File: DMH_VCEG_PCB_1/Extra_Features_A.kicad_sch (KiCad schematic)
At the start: 13 parts, among them U4 CD4066BE, U8 TL074

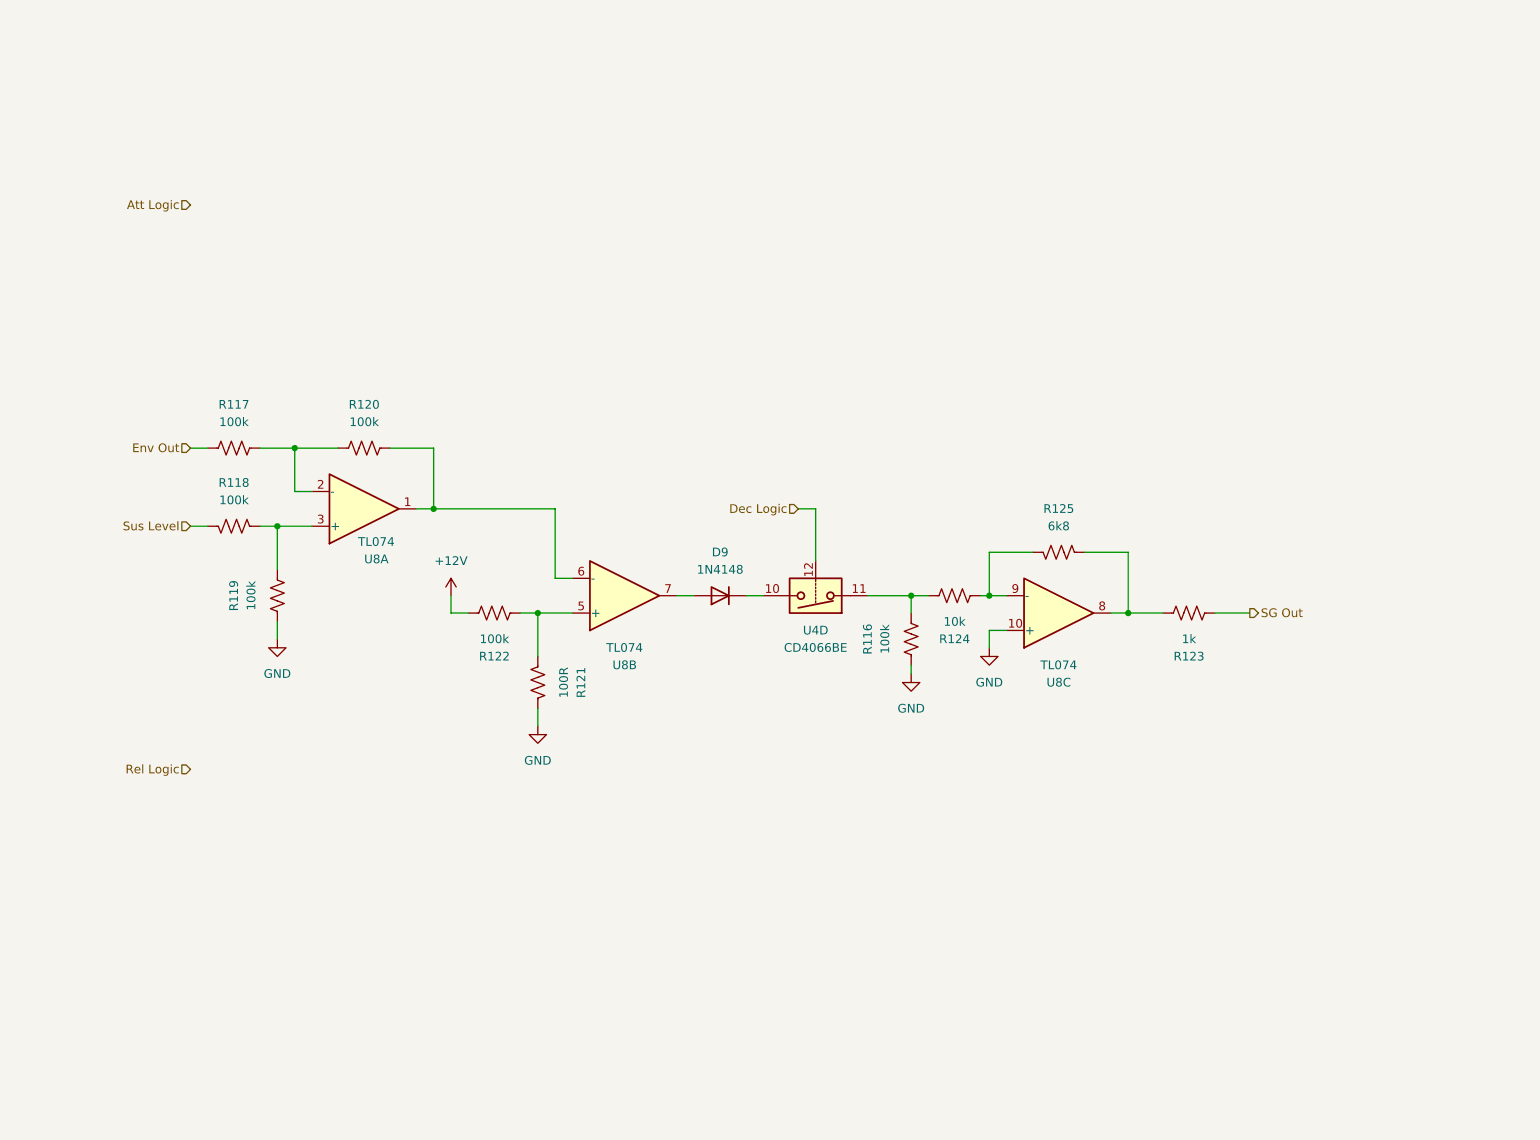
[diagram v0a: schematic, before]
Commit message: Implemented LEDs
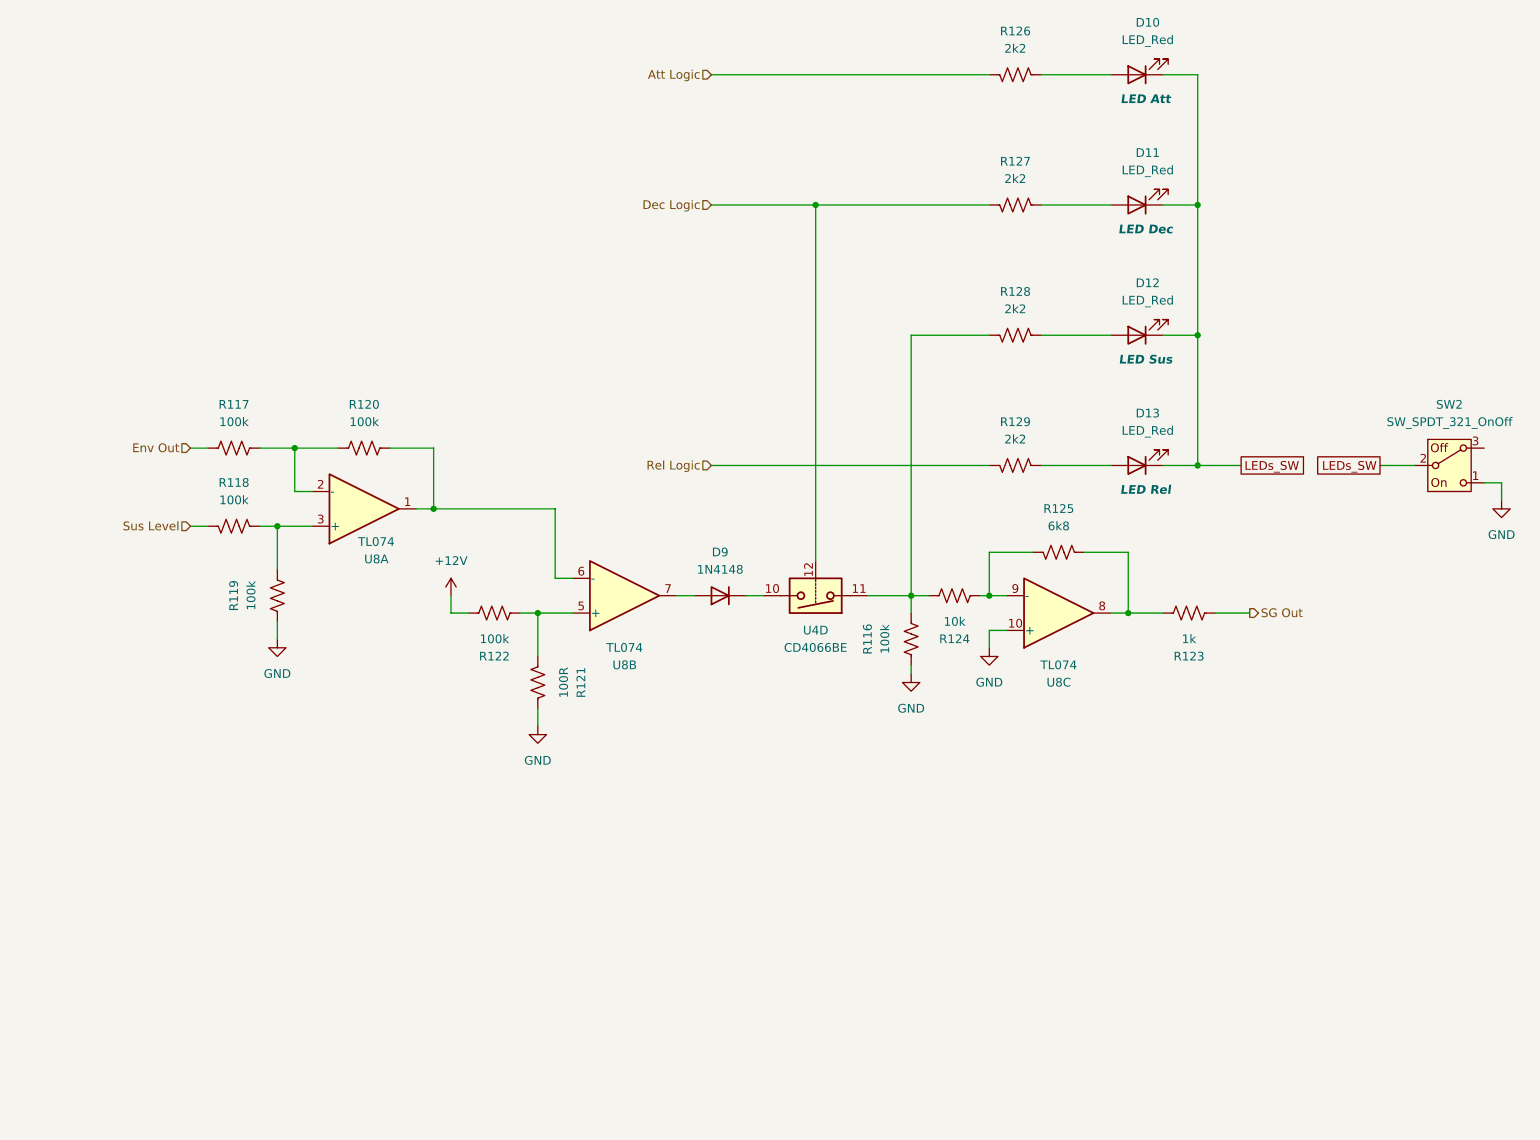
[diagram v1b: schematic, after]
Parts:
- added D10, D11, D12, D13: LED_Red, LED_THT:LED_D3.0mm, symbol Device:LED
- added R126, R127, R128, R129: 2k2, Resistor_THT:R_Axial_DIN0207_L6.3mm_D2.5mm_P7.62mm_Horizontal, symbol Device:R_US
- added SW2: SW_SPDT_321_OnOff, SynthStuff:Toggle_Switch_THT, symbol SynthStuff:SW_SPDT_321_OnOff
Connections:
- net Att Logic: now also R126.1
- net Dec Logic: now also R127.1
- net GND: now also SW2.1 (C)
- net Rel Logic: now also R129.1
- net at R116.1, R124.1, U4.11: now also R128.1
- new net: D10.2 (A), R126.2
- new net: D11.2 (A), R127.2
- new net: D13.2 (A), R129.2
- new net: D12.2 (A), R128.2
- new net LEDs_SW: D10.1 (K), D11.1 (K), D12.1 (K), D13.1 (K), SW2.2 (B)

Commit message: Added Out R
Ready for breadboarding
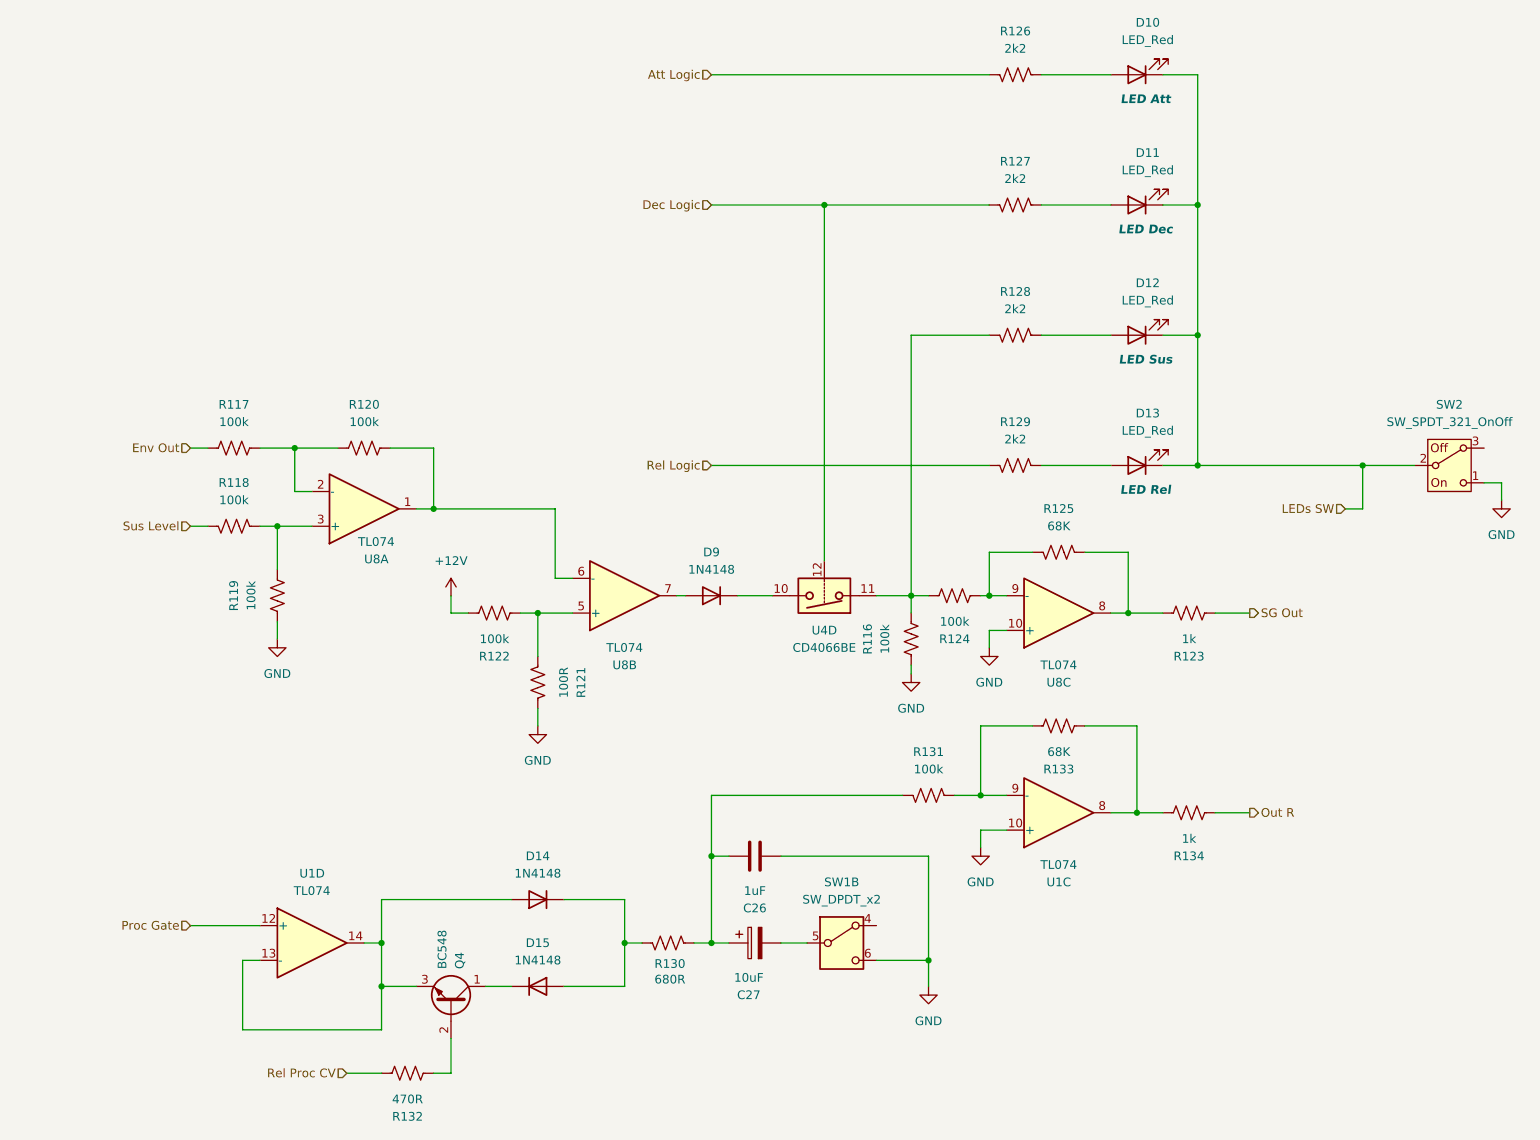
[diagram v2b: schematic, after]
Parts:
- added C26: 1uF, Capacitor_THT:C_Disc_D4.3mm_W1.9mm_P5.00mm, symbol Device:C
- added C27: 10uF, Capacitor_THT:CP_Radial_D5.0mm_P2.00mm, symbol Device:C_Polarized
- added D14, D15: 1N4148, Diode_THT:D_DO-35_SOD27_P7.62mm_Horizontal, symbol Diode:1N4148
- added Q4: BC548, Package_TO_SOT_THT:TO-92L_Inline_Wide, symbol Transistor_BJT:BC548
- added R130: 680R, Resistor_THT:R_Axial_DIN0207_L6.3mm_D2.5mm_P7.62mm_Horizontal, symbol Device:R_US
- added R131: 100k, Resistor_THT:R_Axial_DIN0207_L6.3mm_D2.5mm_P7.62mm_Horizontal, symbol Device:R_US
- added R132: 470R, Resistor_THT:R_Axial_DIN0207_L6.3mm_D2.5mm_P7.62mm_Horizontal, symbol Device:R_US
- added R133: 68K, Resistor_THT:R_Axial_DIN0207_L6.3mm_D2.5mm_P7.62mm_Horizontal, symbol Device:R_US
- added R134: 1k, Resistor_THT:R_Axial_DIN0207_L6.3mm_D2.5mm_P7.62mm_Horizontal, symbol Device:R_US
- added SW1: SW_DPDT_x2, symbol Switch:SW_DPDT_x2
- added U1: TL074, symbol Amplifier_Operational:TL074
- R124: value 10k -> 100k
- R125: value 6k8 -> 68K
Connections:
- net GND: now also C26.2, SW1.6 (C), U1.10 (+)
- net LEDs_SW renamed LEDs SW
- new net: D15.1 (K), Q4.1 (C)
- new net: D14.1 (K), D15.2 (A), R130.2
- new net: C26.1, C27.1, R130.1, R131.1
- new net: C27.2, SW1.5 (B)
- new net: Q4.2 (B), R132.2
- new net: R131.2, R133.1, U1.9 (-)
- new net: D14.2 (A), Q4.3 (E), U1.13 (-), U1.14
- new net: R133.2, R134.1, U1.8
- new net Out R: R134.2
- new net Proc Gate: U1.12 (+)
- new net Rel Proc CV: R132.1
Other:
- moved on the sheet: D9, U4D

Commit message: Corrected Out R design
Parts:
- removed D15: 1N4148, Diode_THT:D_DO-35_SOD27_P7.62mm_Horizontal, symbol Diode:1N4148
- added R2, R4: 100k, Resistor_THT:R_Axial_DIN0207_L6.3mm_D2.5mm_P7.62mm_Horizontal, symbol Device:R_US
- added U3: 40106, symbol 4xxx:40106
- SW2: footprint SynthStuff:Toggle_Switch_THT -> SynthStuff:Toggle_Switch_TE
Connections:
- net GND: now also U1.10 (+), U1.12 (+); no longer U1.10 (+)
- net Proc Gate: now also U3.3; no longer U1.12 (+)
- net at Q4.1 (C): now also D14.1 (K), R130.2
- net at R131.2, R133.1: now also U1.13 (-); no longer U1.9 (-)
- net at D14.2 (A), Q4.3 (E): now also U3.6; no longer U1.13 (-), U1.14
- new net: R134.1, R4.2, U1.8
- new net: R2.2, R4.1, U1.9 (-)
- new net: R133.2, R2.1, U1.14
- new net: U3.4, U3.5
- no-connect marks 0 -> 2
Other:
- moved on the sheet: C26, C27, D14, R130, R131, R133, R134, SW1B, U1C, U1D, U4D
